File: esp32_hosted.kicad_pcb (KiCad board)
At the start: 2 copper layers, 41.5 x 31 mm, 27 parts, among them J1 BT_UART, J2 WIFI, J3 PWR, J4 PROG, SW1 RESET, U1 AP7384-33SA, U2 ESP32-WROOM-32, U3 PCB_SD

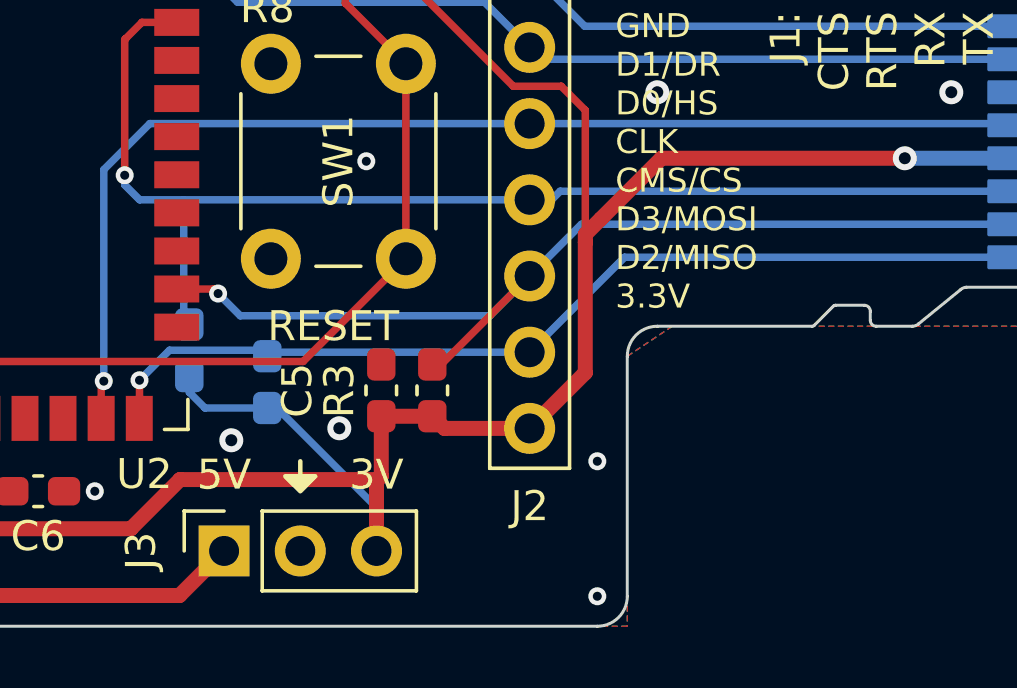
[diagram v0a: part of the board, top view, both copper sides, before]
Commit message: forgot to breakout the reset pin
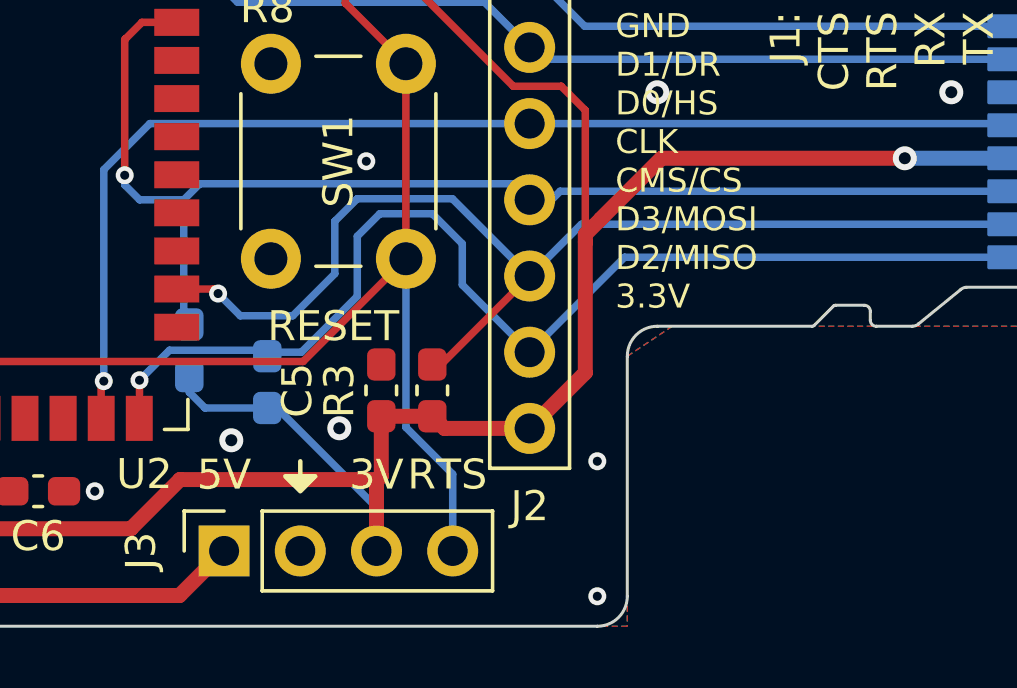
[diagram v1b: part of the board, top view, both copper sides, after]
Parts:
- J3: footprint Connector_PinSocket_2.54mm:PinSocket_1x03_P2.54mm_Vertical -> Connector_PinSocket_2.54mm:PinSocket_1x04_P2.54mm_Vertical
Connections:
- net /P_DTR renamed /BOOT
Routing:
- net /ESP_RTS: track 49.5 -> 59.9 mm
- net /D2/MISO: track 32.9 -> 38.7 mm
- net /D3/MOSI: track 34.6 -> 37.7 mm
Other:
- board text added: "RTS"
